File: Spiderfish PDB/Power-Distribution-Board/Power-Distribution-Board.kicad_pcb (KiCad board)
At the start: 4 copper layers, 100 x 90 mm, 116 parts, among them J1 Conn_01x04_Pin, J10 XT90PB-F, J2 USB_B_Micro, J3 TB002-500-02BE, J4 TB002-500-02BE, J5 TB002-500-02BE, J6 TB002-500-02BE, J7 TB002-500-02BE, J8 TB002-500-02BE, U1 STM32L052K6T6, U10 AOZ2264NQI-11, U11 RT6254BHGJ6F, U12 RT6254BHGJ6F, U4 USBLC6-2SC6, U5 AOZ2264NQI-11, U6 AOZ2264NQI-11, U7 AOZ2264NQI-11, U8 AOZ2264NQI-11, U9 AOZ2264NQI-11

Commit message: refined layout
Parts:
- moved S2 230.3 mm to (75.2, -25.0), turned to -90 degrees
- moved R7 204.8 mm to (60.9, -28.5)
- moved J1 204.3 mm to (75.6, -33.9)
- moved L9 109.3 mm to (-64.8, -28.2)
- moved U11 85.0 mm to (-67.8, -10.8)
- moved C42 83.6 mm to (-88.1, -2.02)
- moved C43 83.6 mm to (-87.5, -17.2)
- moved R39 83.6 mm to (-82.9, -18.0)
- moved C41 83.6 mm to (-87.5, -20.3)
- moved C44 83.6 mm to (-87.5, -14.2)
- moved R38 83.6 mm to (-82.9, -20.5)
- moved R40 83.6 mm to (-82.9, -15.5)
- moved R41 83.6 mm to (-82.9, -13.0)
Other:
- outline, holes or cut-outs redrawn
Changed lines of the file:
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@@
 	(footprint "Connector_PinHeader_2.54mm:PinHeader_1x04_P2.54mm_Vertical"
 		(layer "B.Cu")
-		(at -128.12 -19.085 90)
+		(at 75.6 -33.9 90)
 		(descr "Through hole straight pin header, 1x04, 2.54mm pitch, single row")
 		(tags "Through hole pin header THT 1x04 2.54mm single row")
@@
 	(footprint "Capacitor_SMD:C_0805_2012Metric_Pad1.18x1.45mm_HandSolder"
 		(layer "B.Cu")
-		(at -106.795 64.06 180)
+		(at -87.455 -17.242 180)
 		(descr "Capacitor SMD 0805 (2012 Metric), square (rectangular) end terminal, IPC-7351 nominal with elongated pad for handsoldering. (Body size source: IPC-SM-782 page 76, https://www.pcb-3d.com/wordpress/wp-content/uploads/ipc-sm-782a_amendment_1_and_2.pdf, https://docs.google.com/spreadsheets/d/1BsfQQcO9C6DZCsRaXUlFlo91Tg2WpOkGARC1WS5S8t0/edit?usp=sharing), generated with kicad-footprint-generator")
 		(tags "capacitor handsolder")
@@
 	(footprint "Resistor_SMD:R_0603_1608Metric_Pad0.98x0.95mm_HandSolder"
 		(layer "B.Cu")
-		(at -102.215 65.82 180)
+		(at -82.875 -15.482 180)
 		(descr "Resistor SMD 0603 (1608 Metric), square (rectangular) end terminal, IPC-7351 nominal with elongated pad for handsoldering. (Body size source: IPC-SM-782 page 72, https://www.pcb-3d.com/wordpress/wp-content/uploads/ipc-sm-782a_amendment_1_and_2.pdf), generated with kicad-footprint-generator")
 		(tags "resistor handsolder")
@@
 	(footprint "Resistor_SMD:R_0603_1608Metric_Pad0.98x0.95mm_HandSolder"
 		(layer "B.Cu")
-		(at -102.215 60.8 180)
+		(at -82.875 -20.502 180)
 		(descr "Resistor SMD 0603 (1608 Metric), square (rectangular) end terminal, IPC-7351 nominal with elongated pad for handsoldering. (Body size source: IPC-SM-782 page 72, https://www.pcb-3d.com/wordpress/wp-content/uploads/ipc-sm-782a_amendment_1_and_2.pdf), generated with kicad-footprint-generator")
 		(tags "resistor handsolder")
@@
 	(footprint "Power_Distribution_Board:IHLP-4040DZ-01"
 		(layer "B.Cu")
-		(at -93.24 77.302 180)
+		(at -64.8 -28.2 180)
 		(descr "IHLP4040")
 		(tags "Inductor")
@@
 	(footprint "Capacitor_SMD:C_1206_3216Metric_Pad1.33x1.80mm_HandSolder"
 		(layer "B.Cu")
-		(at -107.395 79.28 180)
+		(at -88.055 -2.022 180)
 		(descr "Capacitor SMD 1206 (3216 Metric), square (rectangular) end terminal, IPC-7351 nominal with elongated pad for handsoldering. (Body size source: IPC-SM-782 page 76, https://www.pcb-3d.com/wordpress/wp-content/uploads/ipc-sm-782a_amendment_1_and_2.pdf), generated with kicad-footprint-generator")
 		(tags "capacitor handsolder")
@@
 	(footprint "Power_Distribution_Board:EG1218"
 		(layer "B.Cu")
-		(at -154.95 -16.085 90)
+		(at 75.2 -25 -90)
 		(descr "EG1218-3")
 		(tags "Switch")
@@
 		(attr through_hole)
 		(fp_line
-			(start 8.3 -2)
-			(end -3.3 -2)
+			(start -3.3 2)
+			(end 8.3 2)
 			(stroke
 				(width 0.1)
@@
 		)
 		(fp_line
-			(start -3.3 -2)
-			(end -3.3 2)
+			(start 8.3 2)
+			(end 8.3 -2)
 			(stroke
 				(width 0.1)
@@
 		)
 		(fp_line
-			(start -4.3 0)
-			(end -4.3 0)
+			(start -4.5 0)
+			(end -4.5 0)
 			(stroke
 				(width 0.2)
@@
 		)
 		(fp_line
-			(start -4.5 0)
-			(end -4.5 0)
+			(start -4.3 0)
+			(end -4.3 0)
 			(stroke
 				(width 0.2)
@@
 		)
 		(fp_line
-			(start 8.3 2)
-			(end 8.3 -2)
+			(start -3.3 -2)
+			(end -3.3 2)
 			(stroke
 				(width 0.1)
@@
 		)
 		(fp_line
-			(start -3.3 2)
-			(end 8.3 2)
+			(start 8.3 -2)
+			(end -3.3 -2)
 			(stroke
 				(width 0.1)
@@
 		)
 		(fp_arc
-			(start -4.3 0)
-			(mid -4.4 0.1)
-			(end -4.5 0)
+			(start -4.5 0)
+			(mid -4.4 -0.1)
+			(end -4.3 0)
 			(stroke
 				(width 0.2)
@@
 		)
 		(fp_arc
-			(start -4.5 0)
-			(mid -4.4 -0.1)
-			(end -4.3 0)
+			(start -4.3 0)
+			(mid -4.4 0.1)
+			(end -4.5 0)
 			(stroke
 				(width 0.2)
@@
 		)
 		(fp_line
-			(start 9.3 -3)
-			(end -5.5 -3)
+			(start -5.5 3)
+			(end 9.3 3)
 			(stroke
 				(width 0.1)
@@
 		)
 		(fp_line
-			(start -5.5 -3)
-			(end -5.5 3)
+			(start 9.3 3)
+			(end 9.3 -3)
 			(stroke
 				(width 0.1)
@@
 		)
 		(fp_line
-			(start 9.3 3)
-			(end 9.3 -3)
+			(start -5.5 -3)
+			(end -5.5 3)
 			(stroke
 				(width 0.1)
@@
 		)
 		(fp_line
-			(start -5.5 3)
-			(end 9.3 3)
+			(start 9.3 -3)
+			(end -5.5 -3)
 			(stroke
 				(width 0.1)
@@
 		)
 		(fp_line
-			(start 8.3 -2)
-			(end -3.3 -2)
+			(start -3.3 2)
+			(end 8.3 2)
 			(stroke
 				(width 0.2)
@@
 		)
 		(fp_line
-			(start -3.3 -2)
-			(end -3.3 2)
+			(start 8.3 2)
+			(end 8.3 -2)
 			(stroke
 				(width 0.2)
@@
 		)
 		(fp_line
-			(start 8.3 2)
-			(end 8.3 -2)
+			(start -3.3 -2)
+			(end -3.3 2)
 			(stroke
 				(width 0.2)
@@
 		)
 		(fp_line
-			(start -3.3 2)
-			(end 8.3 2)
+			(start 8.3 -2)
+			(end -3.3 -2)
 			(stroke
 				(width 0.2)
@@
 		)
 		(pad "1" thru_hole circle
-			(at 0 0 90)
+			(at 0 0 270)
 			(size 1.5 1.5)
 			(drill 1)
@@
 		)
 		(pad "2" thru_hole circle
-			(at 2.5 0 90)
+			(at 2.5 0 270)
 			(size 1.5 1.5)
 			(drill 1)
@@
 		)
 		(pad "3" thru_hole circle
-			(at 5 0 90)
+			(at 5 0 270)
 			(size 1.5 1.5)
 			(drill 1)
@@
 	(footprint "Capacitor_SMD:C_0805_2012Metric_Pad1.18x1.45mm_HandSolder"
 		(layer "B.Cu")
-		(at -106.795 67.07 180)
+		(at -87.455 -14.232 180)
 		(descr "Capacitor SMD 0805 (2012 Metric), square (rectangular) end terminal, IPC-7351 nominal with elongated pad for handsoldering. (Body size source: IPC-SM-782 page 76, https://www.pcb-3d.com/wordpress/wp-content/uploads/ipc-sm-782a_amendment_1_and_2.pdf, https://docs.google.com/spreadsheets/d/1BsfQQcO9C6DZCsRaXUlFlo91Tg2WpOkGARC1WS5S8t0/edit?usp=sharing), generated with kicad-footprint-generator")
 		(tags "capacitor handsolder")
@@
 	(footprint "Resistor_SMD:R_0603_1608Metric_Pad0.98x0.95mm_HandSolder"
 		(layer "B.Cu")
-		(at -102.215 63.31 180)
+		(at -82.875 -17.992 180)
 		(descr "Resistor SMD 0603 (1608 Metric), square (rectangular) end terminal, IPC-7351 nominal with elongated pad for handsoldering. (Body size source: IPC-SM-782 page 72, https://www.pcb-3d.com/wordpress/wp-content/uploads/ipc-sm-782a_amendment_1_and_2.pdf), generated with kicad-footprint-generator")
 		(tags "resistor handsolder")
@@
 	(footprint "Power_Distribution_Board:RT6254BHGJ6F"
 		(layer "B.Cu")
-		(at -111.85 61.87 180)
+		(at -67.8 -10.8 180)
 		(descr "TSOT-23-6 (FC")
 		(tags "Integrated Circuit")
@@
 	(footprint "Capacitor_SMD:C_0805_2012Metric_Pad1.18x1.45mm_HandSolder"
 		(layer "B.Cu")
-		(at -106.795 61.05 180)
+		(at -87.455 -20.252 180)
 		(descr "Capacitor SMD 0805 (2012 Metric), square (rectangular) end terminal, IPC-7351 nominal with elongated pad for handsoldering. (Body size source: IPC-SM-782 page 76, https://www.pcb-3d.com/wordpress/wp-content/uploads/ipc-sm-782a_amendment_1_and_2.pdf, https://docs.google.com/spreadsheets/d/1BsfQQcO9C6DZCsRaXUlFlo91Tg2WpOkGARC1WS5S8t0/edit?usp=sharing), generated with kicad-footprint-generator")
 		(tags "capacitor handsolder")
@@
 	(footprint "Resistor_SMD:R_0603_1608Metric_Pad0.98x0.95mm_HandSolder"
 		(layer "B.Cu")
-		(at -102.215 68.33 180)
+		(at -82.875 -12.972 180)
 		(descr "Resistor SMD 0603 (1608 Metric), square (rectangular) end terminal, IPC-7351 nominal with elongated pad for handsoldering. (Body size source: IPC-SM-782 page 72, https://www.pcb-3d.com/wordpress/wp-content/uploads/ipc-sm-782a_amendment_1_and_2.pdf), generated with kicad-footprint-generator")
 		(tags "resistor handsolder")
@@
 	(footprint "Resistor_SMD:R_0603_1608Metric_Pad0.98x0.95mm_HandSolder"
 		(layer "B.Cu")
-		(at -143.7 -18.9225)
+		(at 60.85 -28.5375)
 		(descr "Resistor SMD 0603 (1608 Metric), square (rectangular) end terminal, IPC-7351 nominal with elongated pad for handsoldering. (Body size source: IPC-SM-782 page 72, https://www.pcb-3d.com/wordpress/wp-content/uploads/ipc-sm-782a_amendment_1_and_2.pdf), generated with kicad-footprint-generator")
 		(tags "resistor handsolder")
@@
 	)
 	(gr_rect
+		(start -50 -15)
+		(end 50 45)
+		(stroke
+			(width 0.05)
+			(type solid)
+		)
+		(fill no)
+		(layer "Edge.Cuts")
+	)
+	(gr_rect

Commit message: rough laytout for all regs, need to increase board size to 10x10
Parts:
- C1: renamed from C42; moved to F.Cu
- C10: renamed from C47; moved to F.Cu
- C11: renamed from C48; moved to F.Cu
- C13: renamed from C36; moved to B.Cu
- C14: renamed from C35; moved to B.Cu
- C2: renamed from C41; moved to F.Cu
- C21: renamed from C14; moved to B.Cu
- C22: renamed from C15; moved to B.Cu
- C23: renamed from C38; moved to B.Cu
- C24: renamed from C37; moved to B.Cu
- C3: renamed from C43; moved to F.Cu
- C30: renamed from C21; moved to B.Cu
- C32: renamed from C23; moved to B.Cu
- C33: renamed from C39; moved to B.Cu
- C34: renamed from C40; moved to B.Cu
- C4: renamed from C44; moved to F.Cu
- C40: renamed from C29; moved to B.Cu
- C42: renamed from C31; moved to B.Cu
- C8: renamed from C45; moved to F.Cu
- C9: renamed from C46; moved to F.Cu
- L1: renamed from L9; moved to F.Cu
- L2: renamed from L1; moved to F.Cu
- R7: renamed from R42; moved to F.Cu
- S1: value TR1-01 -> DS04-254-2-01BK-SMT; footprint Power_Distribution_Board:TR101 -> Power_Distribution_Board:DS04254201BKSMT
- S2: value EG1218 -> CJS-1200TB1; footprint Power_Distribution_Board:EG1218 -> Power_Distribution_Board:CJS1200TB1
- U2: renamed from U11; moved to F.Cu
- U3: renamed from U12; moved to F.Cu
- moved C10 202.0 mm to (23.8, -7.24), turned to -90 degrees
- moved C11 200.9 mm to (21.4, -7.24), turned to -90 degrees
- moved C8 190.7 mm to (9.56, -1.00), turned to 0 degrees
- moved C9 189.9 mm to (14.8, 0.36), turned to -90 degrees
- moved U3 189.7 mm to (11.6, 2.80), turned to 90 degrees
- moved R10 185.1 mm to (11.9, 2.20), turned to 0 degrees
- moved R9 181.6 mm to (8.69, 1.29), turned to 90 degrees
- moved R7 179.4 mm to (10.1, 6.40), turned to 0 degrees
- moved R8 179.3 mm to (8.69, 5.11), turned to 90 degrees
- moved L2 177.5 mm to (13.6, -8.20), turned to 0 degrees
- moved S1 95.5 mm to (102.8, -17.4)
- moved C5 92.6 mm to (-87.1, 19.0)
- moved C6 92.6 mm to (-81.6, 17.2)
- moved C7 92.6 mm to (-91.3, 3.80)
- moved R4 92.6 mm to (-89.0, 1.80)
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- renumbered C7 to C12, C10 to C15, C8 to C16, C11 to C17, C9 to C18, C12 to C19, C13 to C20, C18 to C25, C16 to C26, C19 to C27, C17 to C28, C20 to C29, C22 to C31, C26 to C35, C24 to C36, C27 to C37, C25 to C38, C28 to C39, C30 to C41, C34 to C5, C33 to C6, C32 to C7, J10 to J2, J2 to J3, J3 to J5, J5 to J6, J6 to J7, J7 to J8, J8 to J9, R38 to R1, R45 to R10, R7 to R11, R8 to R12, R9 to R13, R10 to R14, R11 to R15, R12 to R16, R13 to R17, R14 to R18, R15 to R19, R40 to R2, R16 to R20, R17 to R21, R18 to R22, R19 to R23, R20 to R24, R21 to R25, R22 to R26, R23 to R27, R24 to R28, R25 to R29, R39 to R3, R26 to R30, R27 to R31, R28 to R32, R29 to R33, R30 to R34, R31 to R35, R32 to R36, R33 to R37, R34 to R38, R35 to R39, R3 to R4, R36 to R40, R37 to R41, R41 to R5, R5 to R6, R43 to R8, R44 to R9
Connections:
- net Net-(R39-Pad1) renamed /5V0_FB_R
- net Net-(R43-Pad2) renamed /3V3_FB_R
- net Net-(U11-BOOT) renamed /5V0_BOOT
- net Net-(U11-EN) renamed /5V0_EN
- net Net-(U11-FB) renamed /5V0_FB
- net Net-(U11-LX) renamed /5V0_LX
- net Net-(U12-BOOT) renamed /3V3_BOOT
- net Net-(U12-EN) renamed /3V3_EN
- net Net-(U12-FB) renamed /3V3_FB
- net Net-(U12-LX) renamed /3V3_LX
- S1 pad 1: GND -> /NRST
- S2 pad 1: GND -> +3V3
- S2 pad 3: +3V3 -> GND
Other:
- board size 100 x 90 mm -> 100 x 60 mm

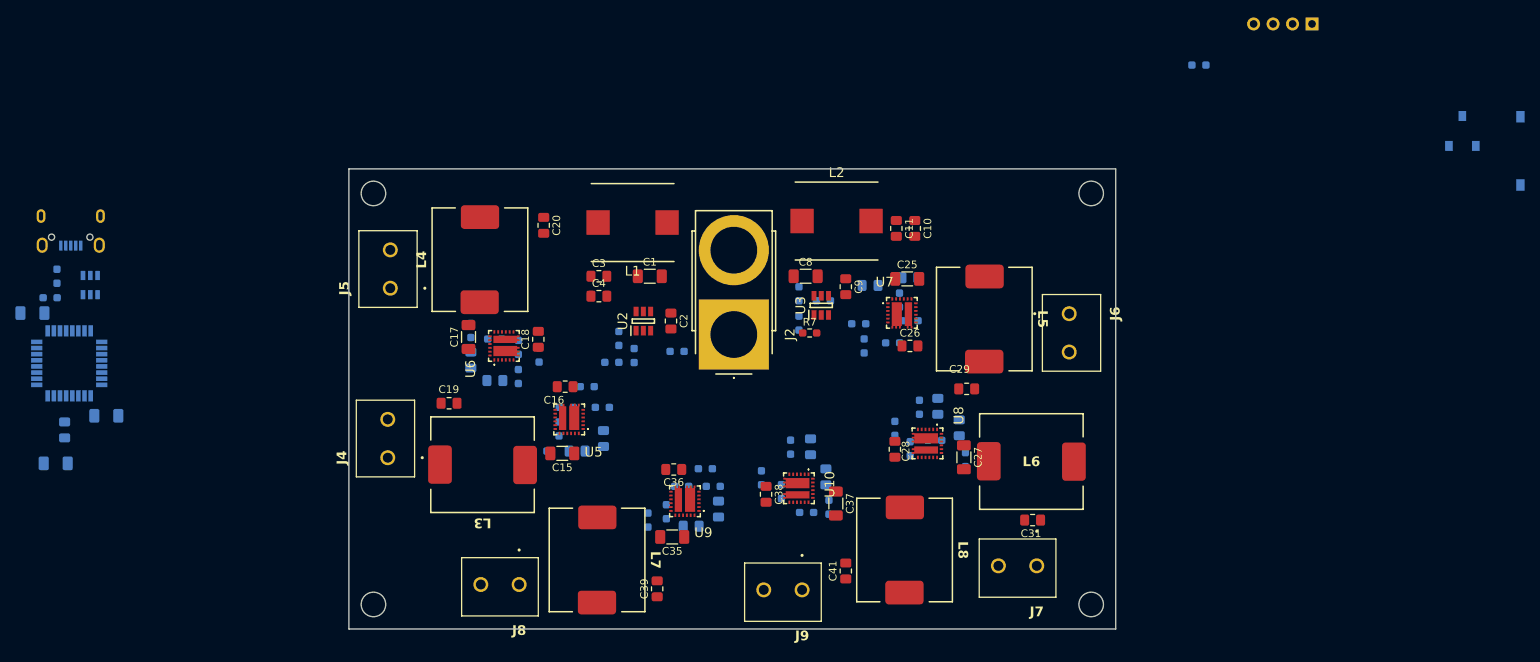
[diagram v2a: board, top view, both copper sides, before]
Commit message: Revision A - changed 3.3V regulator to LDO - all routing done - component selection done
to do:
- update silkscreen placment
- stitching vias
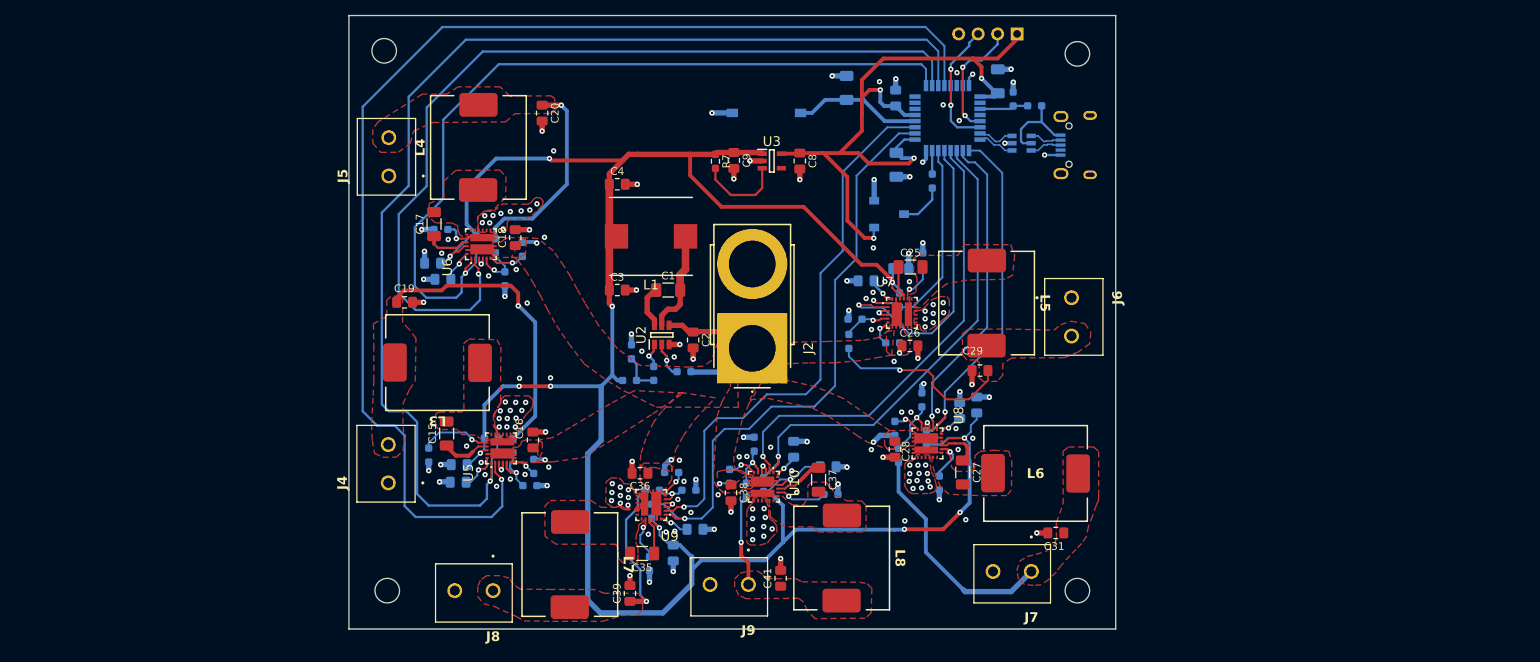
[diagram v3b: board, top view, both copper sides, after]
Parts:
- removed C10, C11: 22u, Capacitor_SMD:C_0805_2012Metric_Pad1.18x1.45mm_HandSolder
- removed L2: 3u3, Power_Distribution_Board:IHLP-4040DZ-01
- removed R10: 20k, Resistor_SMD:R_0603_1608Metric_Pad0.98x0.95mm_HandSolder
- removed R8: 5k, Resistor_SMD:R_0603_1608Metric_Pad0.98x0.95mm_HandSolder
- removed R9: 91k, Resistor_SMD:R_0603_1608Metric_Pad0.98x0.95mm_HandSolder
- C8: value 100n -> 10u; footprint Capacitor_SMD:C_1206_3216Metric_Pad1.33x1.80mm_HandSolder -> Capacitor_SMD:C_0805_2012Metric_Pad1.18x1.45mm_HandSolder
- C9: value 22u -> 10u
- U3: value RT6254BHGJ6F -> MIC5504-3.3YM5-TR; footprint Power_Distribution_Board:RT6254BHGJ6F -> Power_Distribution_Board:MIC5504-3.3YM5-TR
- moved J3 132.4 mm to (45.9, -17.9), turned to -90 degrees
- moved C7 129.5 mm to (34.6, -26.4), turned to 90 degrees
- moved R6 129.4 mm to (39.4, -23.2), turned to 180 degrees
- moved R4 128.2 mm to (36.6, -24.1), turned to 90 degrees
- moved U4 122.9 mm to (37.7, -18.4), turned to 0 degrees
- moved U1 118.9 mm to (28.1, -21.6), turned to 0 degrees
- moved C5 116.7 mm to (21.3, -24.2), turned to 90 degrees
- moved C12 114.2 mm to (14.9, -25.6), turned to 90 degrees
- moved C6 108.1 mm to (21.4, -15.5), turned to -90 degrees
- moved S1 98.5 mm to (4.45, -22.3), turned to -90 degrees
- moved S2 75.5 mm to (20.4, -9.10), turned to 90 degrees
- moved J1 38.5 mm to (37.1, -32.6)
- moved R11 37.9 mm to (26.1, -13.4), turned to 90 degrees
- moved R7 25.5 mm to (-2.20, -16.0), turned to -90 degrees
- moved C9 22.0 mm to (0.20, -16.1)
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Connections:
- C8 pad 1: /3V3_BOOT -> +3V3
- C8 pad 2: /3V3_LX -> GND
- C9 pad 1: +14V8 -> +5V
- R7 pad 1: +14V8 -> +5V
- R7 pad 2: /3V3_EN -> Net-(U3-EN)
- U1 pad 10: /9V_EN_2 -> /12V_EN_1
- U1 pad 11: /12V_EN_2 -> /12V_PGOOD_2
- U1 pad 12: unconnected-(U1-PA6-Pad12) -> /12V_EN_2
- U1 pad 14: /12V_PGOOD_1 -> unconnected-(U1-PB0-Pad14)
- U1 pad 15: /12V_PGOOD_2 -> unconnected-(U1-PB1-Pad15)
- U1 pad 2: unconnected-(U1-PC14-OCS32_IN-Pad2) -> /5V_PGOOD_1
- U1 pad 25: unconnected-(U1-PA15-Pad25) -> /9V_PGOOD_2
- U1 pad 26: /9V_PGOOD_1 -> /9V_EN_2
- U1 pad 27: /9V_PGOOD_2 -> /5V_PGOOD_2
- U1 pad 28: /5V_PGOOD_1 -> /5V_EN_2
- U1 pad 29: /5V_PGOOD_2 -> /9V_EN_1
- U1 pad 3: unconnected-(U1-PC15_OCS32_OUT-Pad3) -> /5V_EN_1
- U1 pad 30: unconnected-(U1-PB7-Pad30) -> /9V_PGOOD_1
- U1 pad 6: /5V_EN_1 -> unconnected-(U1-PA0-Pad6)
- U1 pad 7: /9V_EN_1 -> unconnected-(U1-PA1-Pad7)
- U1 pad 8: /12V_EN_1 -> unconnected-(U1-PA2-Pad8)
- U1 pad 9: /5V_EN_2 -> /12V_PGOOD_1
- U3 pad 1: /3V3_FB -> +5V
- U3 pad 2: /3V3_EN -> GND
- U3 pad 3: GND -> Net-(U3-EN)
- U3 pad 4: +14V8 -> unconnected-(U3-NC-Pad4)
- U3 pad 5: /3V3_LX -> +3V3
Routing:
- net +5V: track 0.00 -> 294.3 mm, vias 0 -> 12
- net /12V_EN_2: track 0.00 -> 162.1 mm, vias 0 -> 1
- net /12V_PGOOD_2: track 0.00 -> 154.8 mm, vias 0 -> 1
- net /12V_EN_1: track 0.00 -> 116.2 mm, vias 0 -> 1
- net /12V_PGOOD_1: track 0.00 -> 107.3 mm, vias 0 -> 1
- net GND: track 0.00 -> 97.0 mm, vias 0 -> 172
- net +3V3: track 0.00 -> 92.5 mm, vias 0 -> 4
- net /5V_PGOOD_1: track 0.00 -> 78.2 mm, vias 0 -> 1
- net /5V_EN_1: track 0.00 -> 72.7 mm, vias 0 -> 1
- net /5V_PGOOD_2: track 0.00 -> 64.1 mm, vias 0 -> 1
- net /5V_EN_2: track 0.00 -> 60.8 mm, vias 0 -> 1
- net /9V_PGOOD_2: track 0.00 -> 46.5 mm, vias 0 -> 1
- net +14V8: track 0.00 -> 45.0 mm, vias 0 -> 6
- net /9V_EN_2: track 0.00 -> 41.2 mm, vias 0 -> 1
- net /9V_EN_1: track 0.00 -> 40.4 mm, vias 0 -> 1
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- added copper zone on F.Cu, net +14V8
- added copper zone on F.Cu, net /12V_LX_1
- added copper zone on F.Cu, net /12V_LX_2
- added copper zone on F.Cu, net /12V_OUT1
- added copper zone on F.Cu, net /12V_OUT_2
- added copper zone on F.Cu, net /5V_LX_1
- added copper zone on F.Cu, net /5V_LX_2
- added copper zone on F.Cu, net /5V_OUT_1
- added copper zone on F.Cu, net /5V_OUT_2
- added copper zone on F.Cu, net /9V_LX_1
- added copper zone on F.Cu, net /9V_LX_2
- added copper zone on F.Cu, net /9V_OUT_1
- added copper zone on F.Cu, net /9V_OUT_2
- added copper zone on F.Cu, net GND
- added copper zone on In1.Cu, net GND
- added copper zone on In2.Cu, net GND
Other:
- board size 100 x 60 mm -> 100 x 80 mm
